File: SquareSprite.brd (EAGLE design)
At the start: 35 x 44.6 mm, 24 parts, among them P1 SPRITE_PIN, P2 SPRITE_PIN, U1 CC430F5137, X1 TCXO_7Z

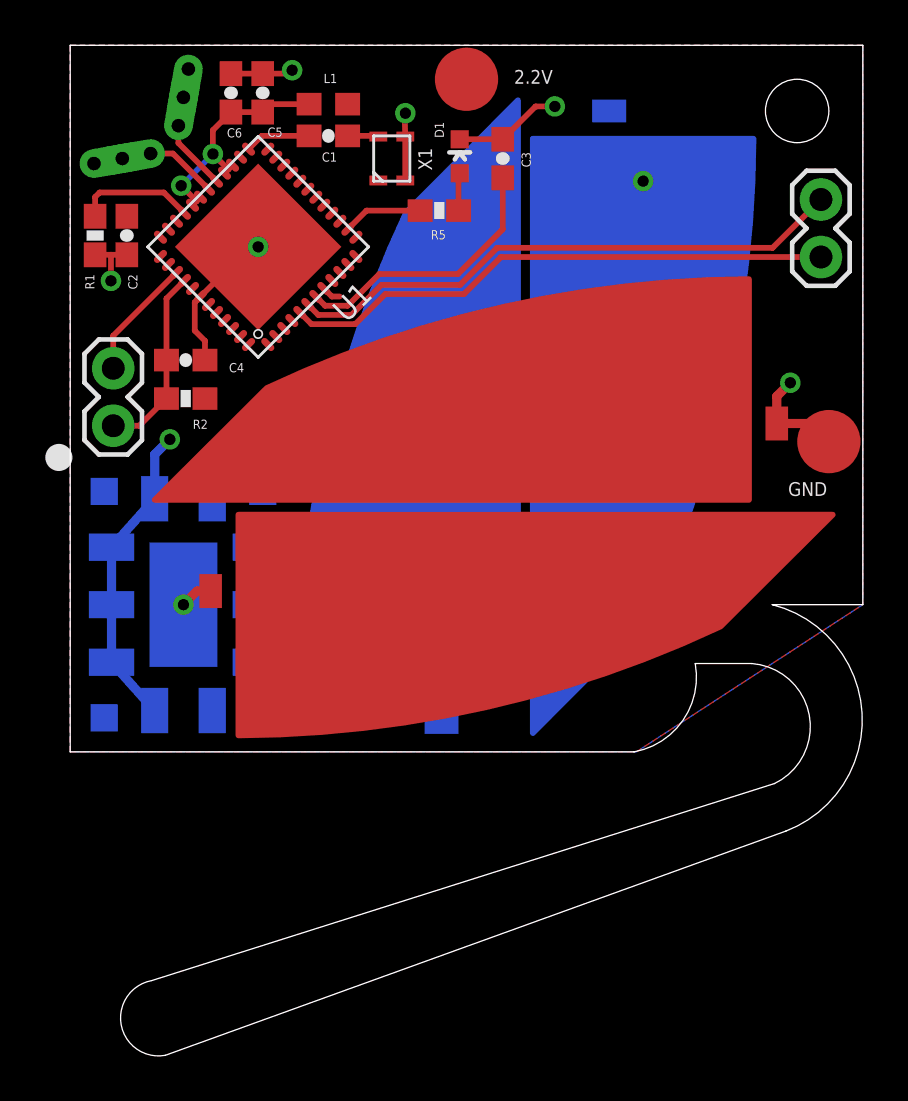
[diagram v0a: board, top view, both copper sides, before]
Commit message: New sprite with spring
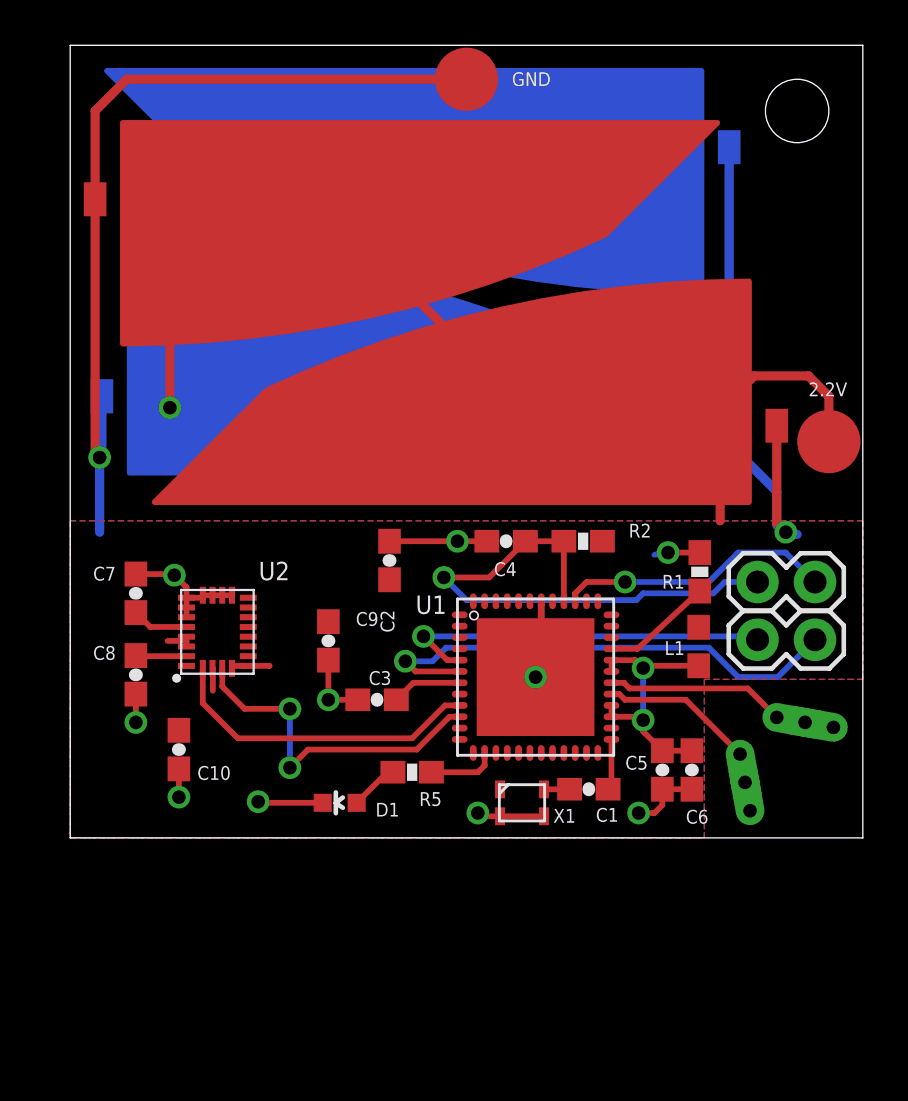
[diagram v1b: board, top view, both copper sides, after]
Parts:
- removed U$1: FASTCAP, FastCap:FASTCAP
- added C10: 10uF, SparkFun:0603-CAP
- added C7: 10nF, SparkFun:0603-CAP
- added C8, C9: 0.1uF, SparkFun:0603-CAP
- added U2: LSM9DS1, LSM9DS1:LGA24-8X4
- moved ANT-P 39.1 mm to (29.8, 2.45), turned to 100 degrees
- moved ANT-N 39.1 mm to (32.5, 5.10), turned to 170 degrees
- moved C6 36.2 mm to (27.4, 3.00), turned to 270 degrees
- moved C5 34.7 mm to (26.1, 3.00), turned to 270 degrees
- moved S2 32.6 mm to (2.20, 31.7), turned to 180 degrees
- moved C1 31.1 mm to (22.9, 2.15), turned to 180 degrees
- moved R1 30.6 mm to (27.8, 11.8), turned to 90 degrees
- moved JP2 29.3 mm to (30.4, 11.3), turned to 0 degrees
- moved D1 29.0 mm to (11.9, 1.55), turned to 90 degrees
- moved X1 29.0 mm to (19.9, 1.55), turned to 0 degrees
- moved L1 29.0 mm to (27.8, 8.45), turned to 270 degrees
- moved R5 24.8 mm to (15.1, 2.90), turned to 0 degrees
- moved C3 24.5 mm to (13.6, 6.10), turned to 180 degrees
- moved S1 22.8 mm to (30.1, 14.7), turned to 0 degrees
- moved U1 22.6 mm to (20.6, 7.10), turned to 0 degrees
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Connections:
- new net N$5: C7.1, U2.21
- new net N$6: C8.1, U2.24
- net GND: now also C10.2, C7.2, C8.2, C9.2, P1.PIN, U2.14, U2.15, U2.16, U2.17, U2.18, U2.19, U2.20; no longer P2.PIN, U$1.P11, U$1.P5, U$1.P6, U$1.P7, U$1.P8, U$1.P9
- net SCL: now also U2.2
- net SDA: now also U2.4
- net VCC: now also C10.1, C9.1, P2.PIN, U2.1, U2.22, U2.23, U2.3, U2.5, U2.6, U2.7, U2.8; no longer P1.PIN, U$1.P1, U$1.P10, U$1.P2, U$1.P3, U$1.P4
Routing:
- net GND: track 25.9 -> 93.2 mm, vias 7 -> 12
- net VCC: track 37.8 -> 86.6 mm, vias 2 -> 1
- net SDA: track 0.00 -> 15.2 mm, vias 0 -> 2
- net RST: track 8.39 -> 23.2 mm, vias 0 -> 1
- net SCL: track 0.00 -> 14.1 mm
- net N$4: track 12.1 -> 3.11 mm
- net UART_TX: track 24.5 -> 16.8 mm, vias 0 -> 1
- net TEST: track 5.39 -> 12.2 mm, vias 0 -> 1
- net RFN: track 5.75 -> 11.7 mm
- net RFP: track 5.69 -> 10.6 mm
- net UART_RX: track 25.0 -> 22.1 mm, vias 0 -> 1
- net N$5: track 0.00 -> 2.50 mm
- net N$6: track 0.00 -> 2.25 mm
- net VCCRF: track 10.7 -> 11.8 mm
- net N$1: track 2.92 -> 2.26 mm
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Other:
- board size 35 x 44.6 mm -> 35 x 35 mm
